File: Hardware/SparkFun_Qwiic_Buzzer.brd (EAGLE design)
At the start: 25.4 x 25.4 mm, 58 parts, among them J2 QWIIC_RA, J3 QWIIC_RA, Q3 200mA/40V, U4 ATTINY84-ARDUINO

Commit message: Layout done
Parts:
- removed LOGO3: SFE_LOGO_NAME.1_INCH, SparkFun-Aesthetics:SFE_LOGO_NAME_.1
- removed U$4: (no value), Labels:INT-()-04
- added LOGO2: SFE_LOGO_NAME_FLAME.1_INCH, SparkFun-Aesthetics:SFE_LOGO_NAME_FLAME_.1
- added R9: USER, SparkFun-Resistors:AXIAL-0.3
- added U$15: (no value), output:##TRIG##6
- added U$21: (no value), output:#INT#10
- added U$5: (no value), output:#USER#1
- added U$6: (no value), output:#PWR#4
- added U$7: (no value), output:#STAT#3
- added U$8: (no value), output:#MISO#8
- U$12: device SparkFun-Aesthetics:QWIIC_4MM -> output:##RST##7
- moved U$14 32.1 mm to (12.7, 7.79)
- moved U$16 32.1 mm to (12.8, 9.91)
- moved LOGO4 27.6 mm to (20.4, 8.19)
- moved LOGO1 25.9 mm to (2.54, 18.7)
- moved U$12 16.0 mm to (11.4, 21.6), flipped to the bottom, turned to 90 degrees
- moved U$10 3.59 mm to (19.1, 24.1), turned to 0 degrees
- moved JP3 3.25 mm to (22.8, 9.56)
- moved U$11 3.19 mm to (22.9, 12.8)
- moved R14 2.78 mm to (19.4, 16.8)
- moved INT 2.20 mm to (19.8, 7.62), turned to 90 degrees
- moved PWR 2.14 mm to (2.86, 6.99), turned to 90 degrees
- moved Q2 2.02 mm to (18.6, 21.8)
- moved R15 1.35 mm to (20.3, 19.4), turned to 0 degrees
- moved R7 1.27 mm to (4.37, 16.4)
- moved R17 1.04 mm to (23.0, 17.2), turned to 180 degrees
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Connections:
- removed net STAT: U4.10
- net N$15: now also R9.P$1
- net N$4: now also R9.P$2
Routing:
- net 3.3V: track 0.00 -> 56.7 mm, vias 0 -> 5
- net SCL: track 0.00 -> 40.0 mm, vias 0 -> 1
- net SDA: track 0.00 -> 39.2 mm
- net MISO: track 0.00 -> 27.6 mm, vias 0 -> 2
- net !RST: track 0.00 -> 26.7 mm, vias 0 -> 2
- net N$10: track 0.00 -> 18.3 mm
- net N$4: track 0.00 -> 17.8 mm
- net N$12: track 0.00 -> 17.6 mm
- net TRIGGER: track 0.00 -> 17.4 mm, vias 0 -> 1
- net N$2: track 0.00 -> 17.1 mm, vias 0 -> 2
- net GND: track 0.00 -> 16.8 mm, vias 0 -> 32
- net N$14: track 0.00 -> 15.5 mm, vias 0 -> 2
- net VOL_3: track 0.00 -> 14.7 mm, vias 0 -> 2
- net VOL_2: track 0.00 -> 13.6 mm, vias 0 -> 2
- net N$11: track 0.00 -> 12.5 mm
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
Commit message: updated miso to poci
both net names and board header silk
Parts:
- removed U$8: (no value), output:#MISO#8
- added U$4: (no value), output:#POCI#11
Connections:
- net MISO renamed POCI
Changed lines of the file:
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@@
 <element name="U$12" library="output" package="##RST##7" value="" x="11.43" y="21.59" smashed="yes" rot="MR90"/>
 <element name="U$15" library="output" package="##TRIG##6" value="" x="13.97" y="21.336" smashed="yes" rot="MR90"/>
-<element name="U$8" library="output" package="#MISO#8" value="" x="8.89" y="21.2725" smashed="yes" rot="MR90"/>
 <element name="U$21" library="output" package="#INT#10" value="" x="19.728178125" y="10.3911375" smashed="yes" rot="MR90"/>
 <element name="LOGO2" library="SparkFun-Aesthetics" package="SFE_LOGO_NAME_FLAME_.1" value="SFE_LOGO_NAME_FLAME.1_INCH" x="12.8905" y="12.446" smashed="yes" rot="MR0"/>
+<element name="U$4" library="output" package="#POCI#11" value="" x="8.89761875" y="21.32838125" smashed="yes" rot="MR90"/>
 </elements>
 <signals>
@@
 <wire x1="3.298" y1="7.9255" x2="2.8575" y2="7.485" width="0.2032" layer="1"/>
 </signal>
-<signal name="MISO">
+<signal name="POCI">
 <contactref element="U4" pad="8"/>
 <contactref element="J4" pad="1"/>

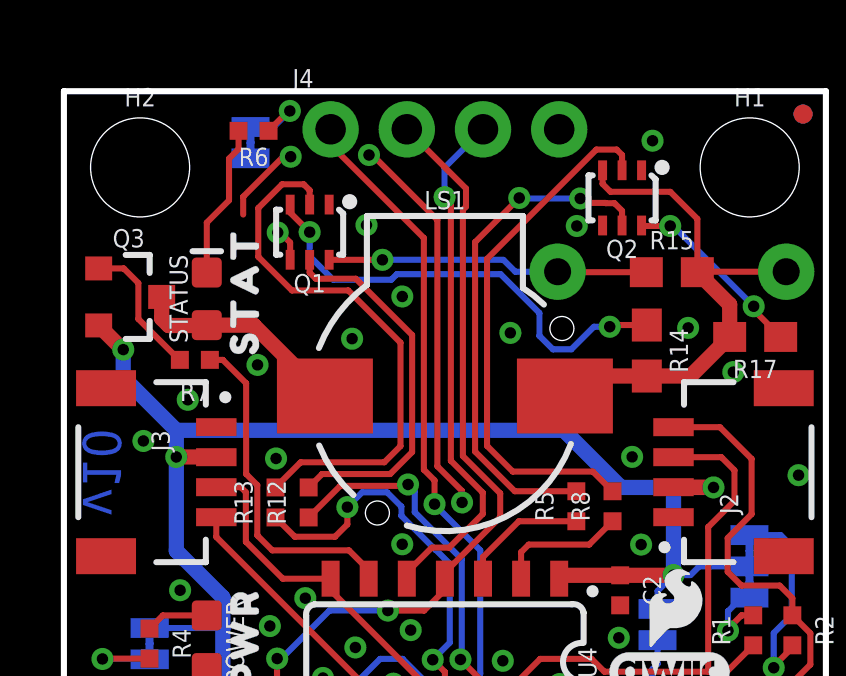
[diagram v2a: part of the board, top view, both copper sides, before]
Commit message: Aligned header to be breadboard friendly
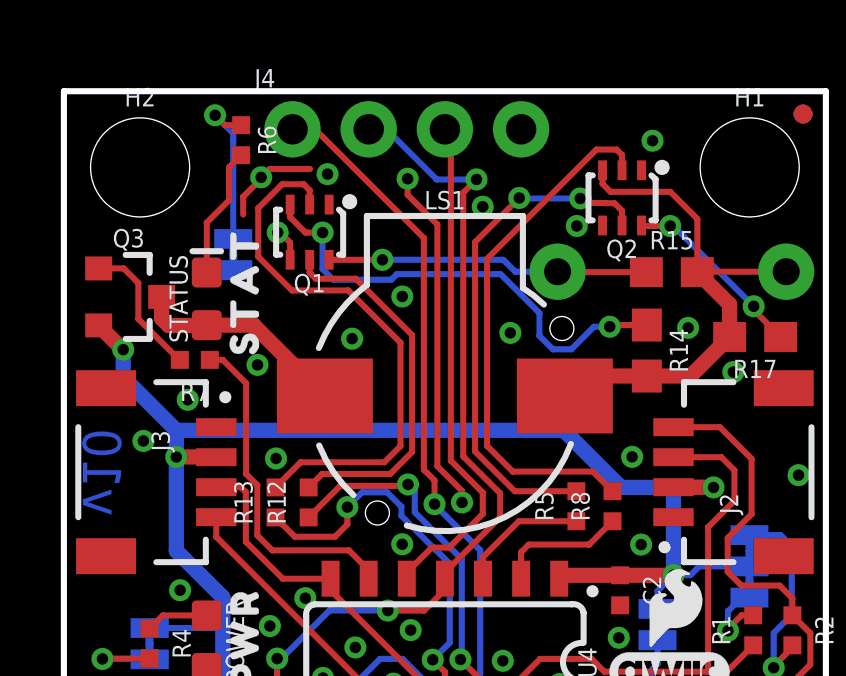
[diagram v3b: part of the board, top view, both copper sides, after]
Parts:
- moved STAT 3.78 mm to (5.64, 20.0)
- moved U$7 3.77 mm to (5.61, 16.3)
- moved U$15 1.27 mm to (12.7, 21.3)
- moved J4 1.27 mm to (7.62, 24.1)
- moved U$10 1.27 mm to (17.8, 24.1)
- moved U$12 1.27 mm to (10.2, 21.6)
- moved U$4 1.27 mm to (7.63, 21.3)
- moved R6 0.52 mm to (5.91, 23.8), turned to 270 degrees
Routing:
- net N$8: track 2.51 -> 5.38 mm
- net !RST: track 26.7 -> 28.6 mm, vias 2 -> 3
- net POCI: track 27.6 -> 28.5 mm
- net GND: track 16.8 -> 15.9 mm, vias 32 -> 33
- net N$7: track 5.16 -> 4.39 mm
- net TRIGGER: track 17.4 -> 16.9 mm, vias 1 -> 0

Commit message: add ordering instructions
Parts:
- added LOGO3: SPECIAL_INSTRUCTIONS-ORDERING, SparkFun-Aesthetics:ORDERING_INSTRUCTIONS
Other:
- board text added: "Thickness: 1.6mm Layers: 2 Solder Mask Color: Red Silkscreen: White Finish: Lead-Free HASL"
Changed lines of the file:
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@@
 <drawing>
 <settings>
-<setting alwaysvectorfont="yes"/>
+<setting alwaysvectorfont="no"/>
 <setting keepoldvectorfont="yes"/>
 <setting verticaltext="up"/>
@@
 <rectangle x1="17.78" y1="18.669" x2="18.161" y2="20.1295" layer="22"/>
 <rectangle x1="22.4155" y1="18.669" x2="22.86" y2="20.066" layer="22"/>
+<text x="58.928" y="42.037" size="2.032" layer="51" font="vector" align="top-left">Thickness: 1.6mm
+Layers: 2
+Solder Mask Color: Red
+Silkscreen: White
+Finish: Lead-Free HASL</text>
 </plain>
 <attributes>
@@
 <element name="LOGO2" library="SparkFun-Aesthetics" package="SFE_LOGO_NAME_FLAME_.1" value="SFE_LOGO_NAME_FLAME.1_INCH" x="12.8905" y="12.446" smashed="yes" rot="MR0"/>
 <element name="U$4" library="output" package="#POCI#11" value="" x="7.62761875" y="21.32838125" smashed="yes" rot="MR90"/>
+<element name="LOGO3" library="SparkFun-Aesthetics" package="ORDERING_INSTRUCTIONS" value="SPECIAL_INSTRUCTIONS-ORDERING" x="57.15" y="53.34" smashed="yes"/>
 </elements>
 <signals>
@@
 </drawing>
 <compatibility>
+<note version="6.3" minversion="6.2.2" severity="warning">
+Since Version 6.2.2 text objects can contain more than one line,
+which will not be processed correctly with this version.
+</note>
 <note version="8.3" severity="warning">
 Since Version 8.3, EAGLE supports URNs for individual library

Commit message: text only label for USER resistor
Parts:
- removed U$5: (no value), output:#USER#1
- added U$8: (no value), output:USER12
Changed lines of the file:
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@@
 <drawing>
 <settings>
-<setting alwaysvectorfont="no"/>
+<setting alwaysvectorfont="yes"/>
 <setting keepoldvectorfont="yes"/>
 <setting verticaltext="up"/>
@@
 <dimension x1="25.4" y1="0" x2="25.4" y2="25.4" x3="29.21" y3="12.7" textsize="1.778" layer="47" unit="inch"/>
 <text x="5.207" y="26.162" size="1.27" layer="47" font="vector">Units in Inches</text>
-<rectangle x1="17.78" y1="18.669" x2="18.161" y2="20.1295" layer="22"/>
-<rectangle x1="22.4155" y1="18.669" x2="22.86" y2="20.066" layer="22"/>
 <text x="58.928" y="42.037" size="2.032" layer="51" font="vector" align="top-left">Thickness: 1.6mm
 Layers: 2
@@
 <attribute name="VALUE" x="20.2666625" y="20.398740625" size="0.6096" layer="28" font="vector" ratio="20" rot="MR180" align="top-center"/>
 </element>
-<element name="U$5" library="output" package="#USER#1" value="" x="20.2565" y="19.3675" smashed="yes" rot="MR0"/>
 <element name="U$7" library="output" package="#STAT#3" value="" x="5.60831875" y="16.34998125" smashed="yes" rot="MR90"/>
 <element name="U$6" library="output" package="#PWR#4" value="" x="2.8575" y="10.16" smashed="yes" rot="MR90"/>
@@
 <element name="U$4" library="output" package="#POCI#11" value="" x="7.62761875" y="21.32838125" smashed="yes" rot="MR90"/>
 <element name="LOGO3" library="SparkFun-Aesthetics" package="ORDERING_INSTRUCTIONS" value="SPECIAL_INSTRUCTIONS-ORDERING" x="57.15" y="53.34" smashed="yes"/>
+<element name="U$8" library="output" package="USER12" value="" x="20.23871875" y="19.395440625" smashed="yes" rot="MR0"/>
 </elements>
 <signals>
